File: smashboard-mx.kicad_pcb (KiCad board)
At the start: 2 copper layers, 139.1 x 76.2 mm, 81 parts, among them J1 OLED_128x32_Nice_View, SW1 SW_SPDT, SW2 SW_Push, SW3 SW_SPDT, SW4 SW_Push, U1 Nice_Nano_V2

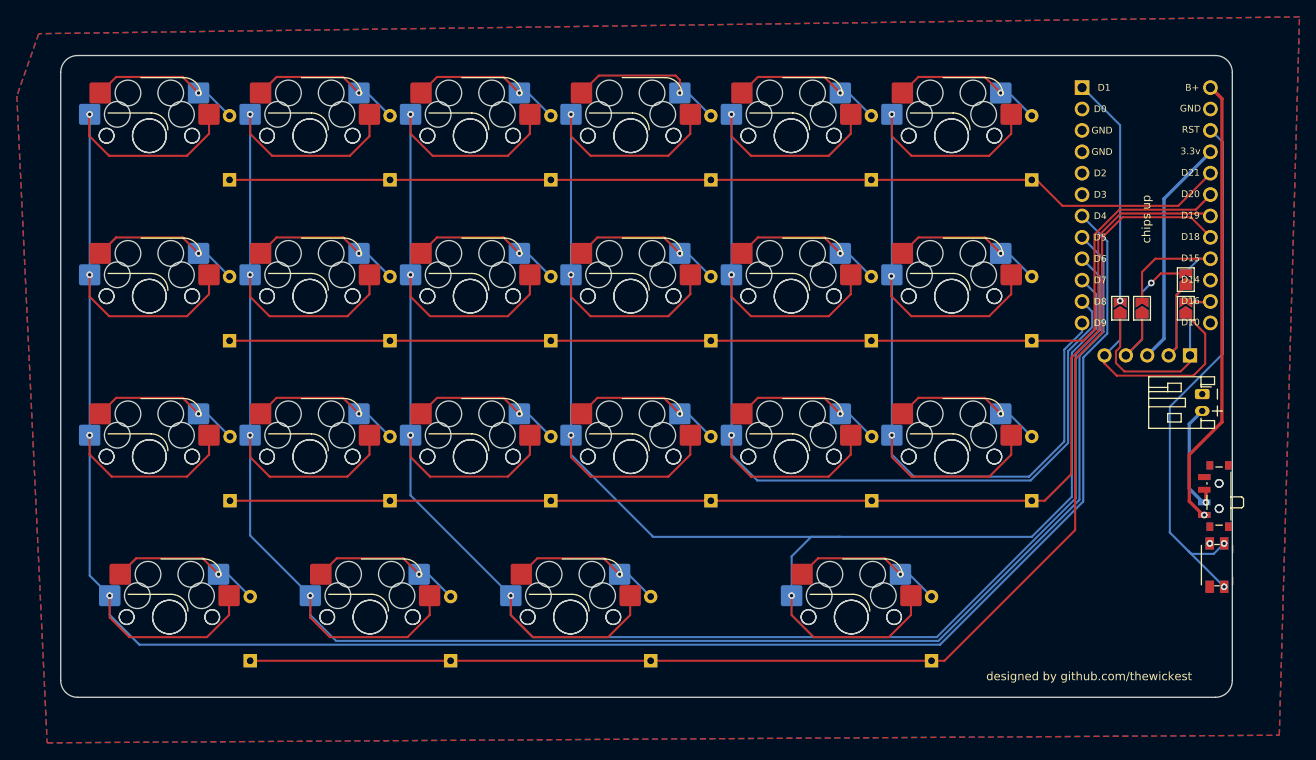
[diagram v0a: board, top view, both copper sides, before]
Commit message: Add M2 holes into the PCB
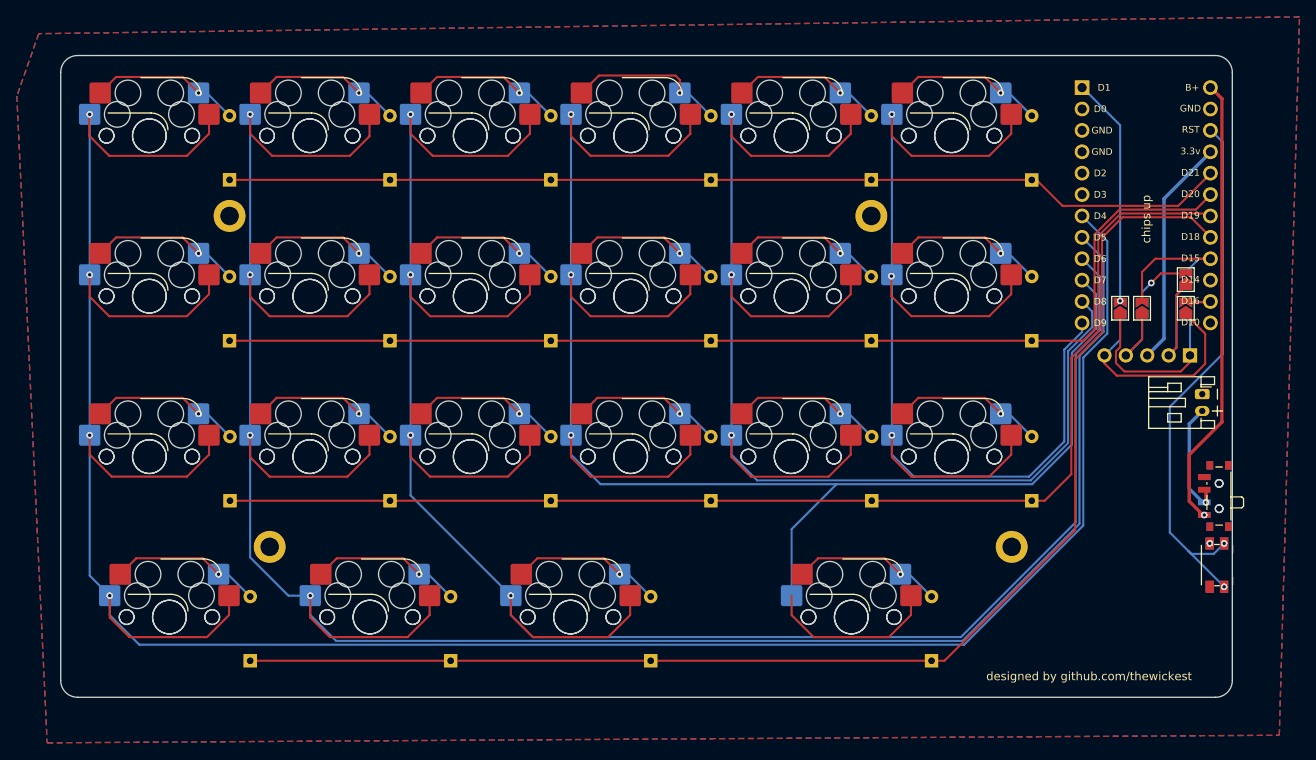
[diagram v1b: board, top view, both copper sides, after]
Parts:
- added REF**: MountingHole_2.2mm_M2_DIN965_Pad, MountingHole:MountingHole_2.2mm_M2_DIN965_Pad, F.Cu at (194.6, 112.6)
- added REF**: MountingHole_2.2mm_M2_DIN965_Pad, MountingHole:MountingHole_2.2mm_M2_DIN965_Pad, F.Cu at (178.0, 73.3)
- added REF**: MountingHole_2.2mm_M2_DIN965_Pad, MountingHole:MountingHole_2.2mm_M2_DIN965_Pad, F.Cu at (106.5, 112.6)
- added REF**: MountingHole_2.2mm_M2_DIN965_Pad, MountingHole:MountingHole_2.2mm_M2_DIN965_Pad, F.Cu at (101.8, 73.3)
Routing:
- net Column4: track 229.1 -> 224.4 mm, vias 4 -> 3
- net Column2: track 279.8 -> 283.0 mm
- net Column3: track 254.0 -> 255.7 mm
- net Column1: track 305.0 -> 306.7 mm

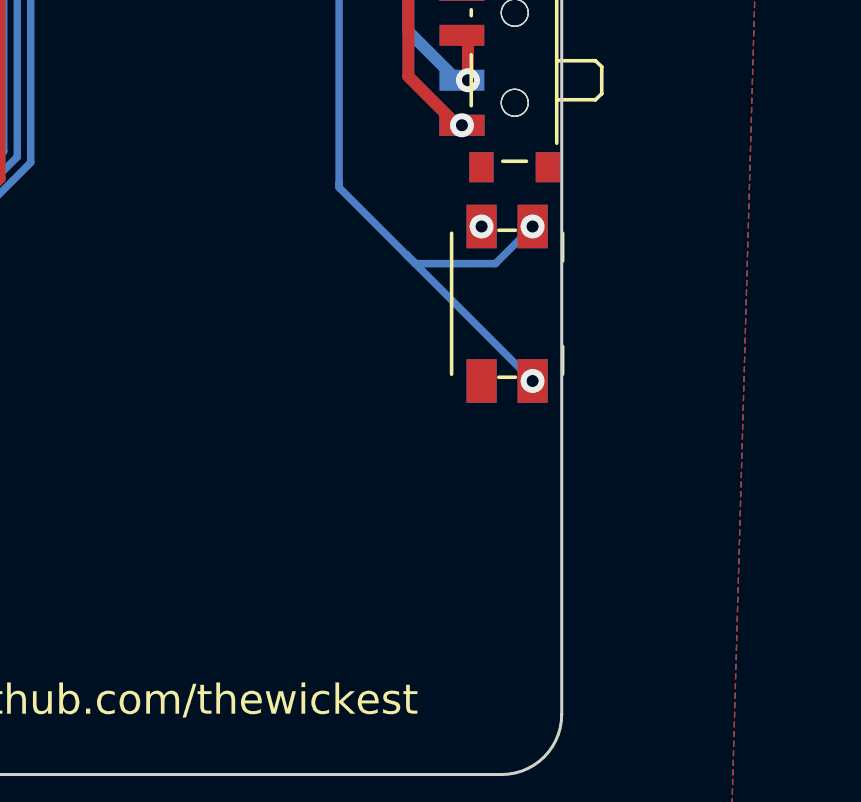
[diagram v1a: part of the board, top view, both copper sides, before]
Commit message: Move reset button
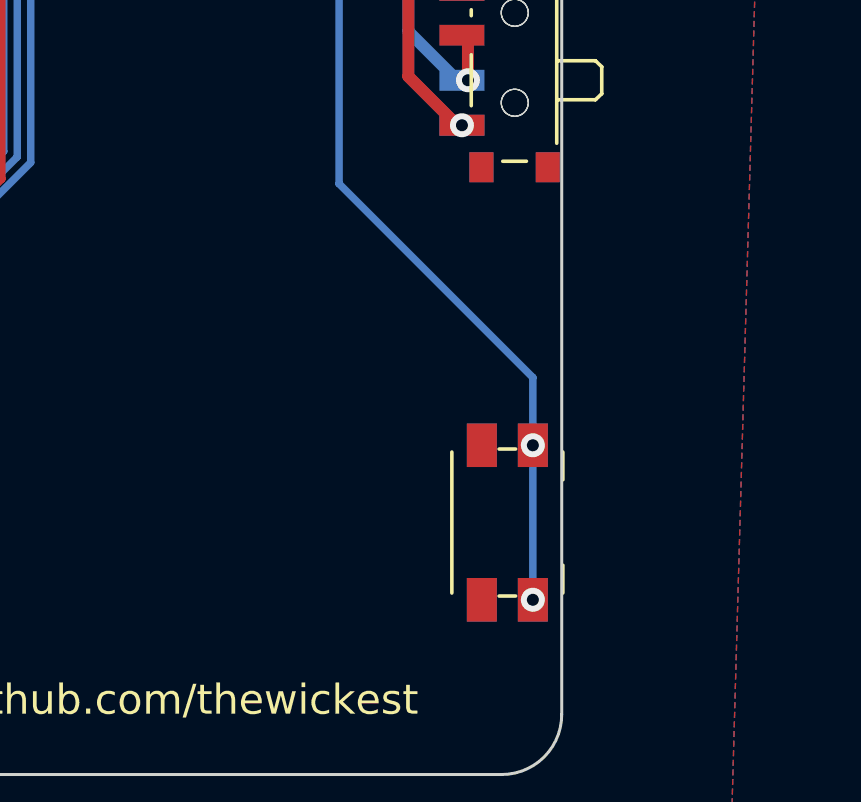
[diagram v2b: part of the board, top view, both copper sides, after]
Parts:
- moved SW2 7.29 mm to (219.0, 122.1)
- moved SW4 7.29 mm to (219.0, 122.1)
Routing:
- net RST: track 64.9 -> 67.4 mm
- net GND: vias 2 -> 1

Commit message: Add Logo and name
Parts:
- added G***: LOGO, SmashBoardLibrary:SmashBoardLogo, F.Cu at (207.5, 115.5)
- added G***: LOGO, SmashBoardLibrary:SmashBoardLogo, B.Cu at (207.5, 115.5)
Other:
- board text added: "smash-b"

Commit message: Production files
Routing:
- net Column4: vias 3 -> 4
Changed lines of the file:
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@@
     (fp_line (start 3.95 6.25) (end 3.95 -1.35)
       (stroke (width 0.1) (type solid)) (layer "F.Fab"))
-    (pad "1" thru_hole roundrect (at 0 0 270) (size 1.2 1.75) (drill 0.75) (layers "*.Cu" "*.Mask") (roundrect_rratio 0.208333)
+    (pad "1" thru_hole roundrect (at 0 0 270) (size 1.2 1.75) (drill 0.75) (layers "*.Cu" "*.Mask") (roundrect_rratio 0.2083333333)
       (net 51 "GND") (pinfunction "GND") (pintype "passive"))
     (pad "2" thru_hole oval (at 2 0 270) (size 1.2 1.75) (drill 0.75) (layers "*.Cu" "*.Mask")
@@
   (via (at 142.29875 80.3275) (size 0.8) (drill 0.4) (layers "F.Cu" "B.Cu") (net 28))
   (via (at 142.29875 99.3775) (size 0.8) (drill 0.4) (layers "F.Cu" "B.Cu") (net 28))
+  (via (at 168.4925 118.4275) (size 0.8) (drill 0.4) (layers "F.Cu" "B.Cu") (net 28))
   (via (at 142.29875 61.2775) (size 0.8) (drill 0.4) (layers "F.Cu" "B.Cu") (net 28))
   (segment (start 142.29875 101.680267) (end 145.810983 105.1925) (width 0.25) (layer "B.Cu") (net 28))
